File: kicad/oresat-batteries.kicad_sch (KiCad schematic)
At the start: 13 parts, among them J1 J-SAMTEC-TFM-120-X1-XXX-D-RA, SW1 Omron D2F-L3-D (LEFT), SW2 Omron D2F-L3-D (RIGHT), SW3 OMRON D2F-L3-D (LEFT), SW4 OMRON D2F-L3-D (RIGHT)

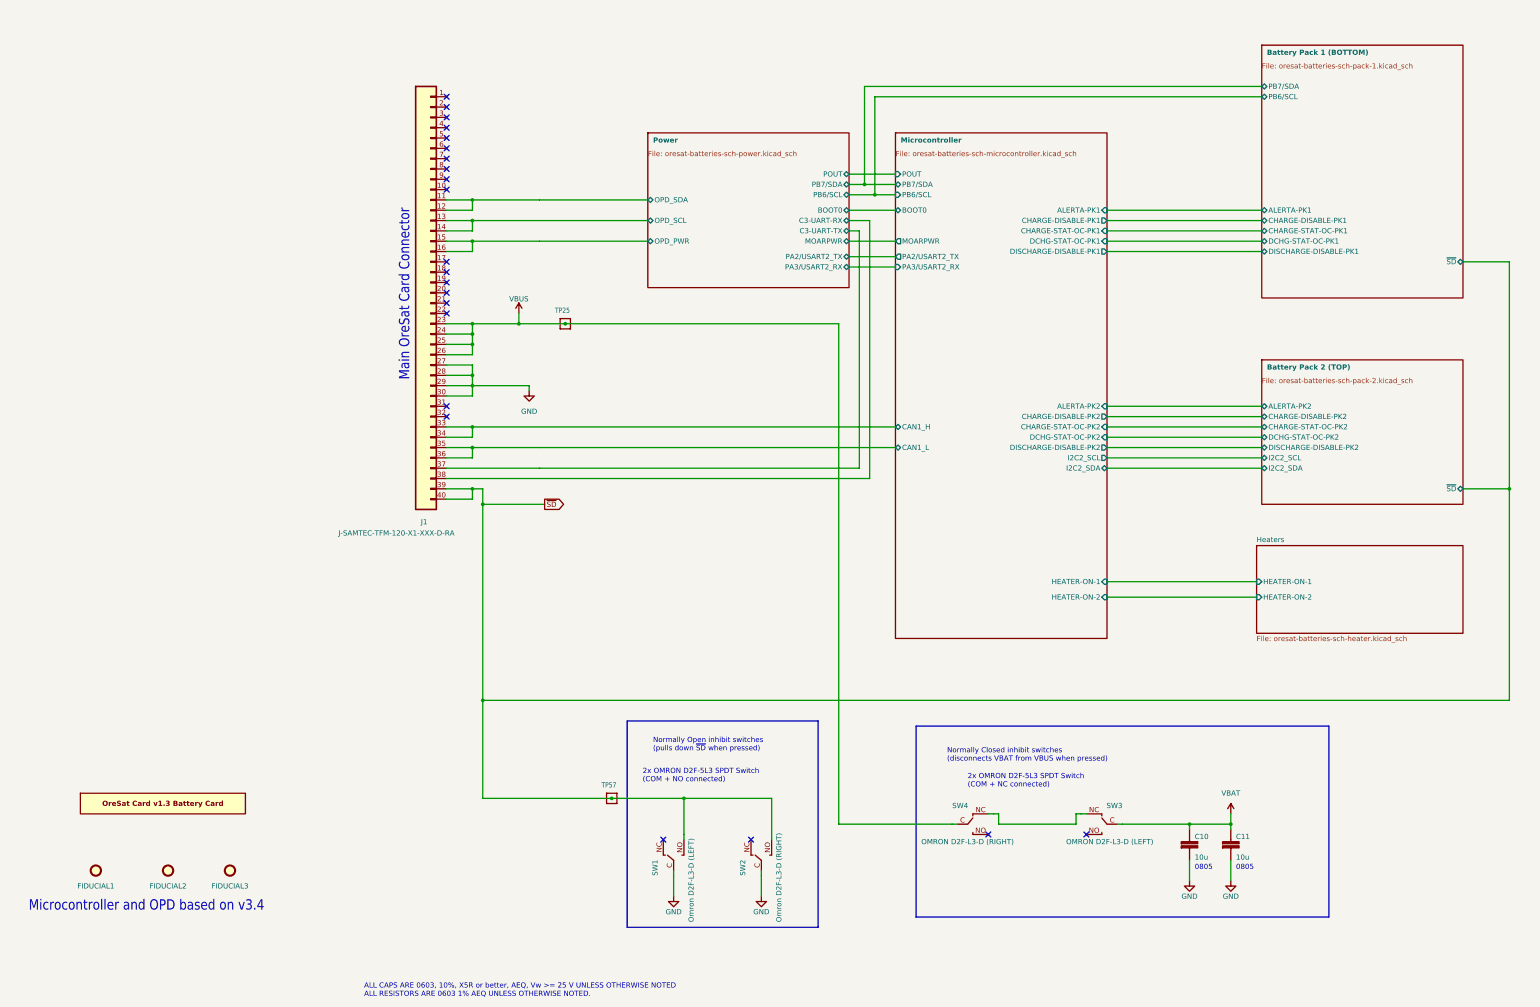
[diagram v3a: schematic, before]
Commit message: Minor polishing, removing outdated OPD signals and OPD power jumper.
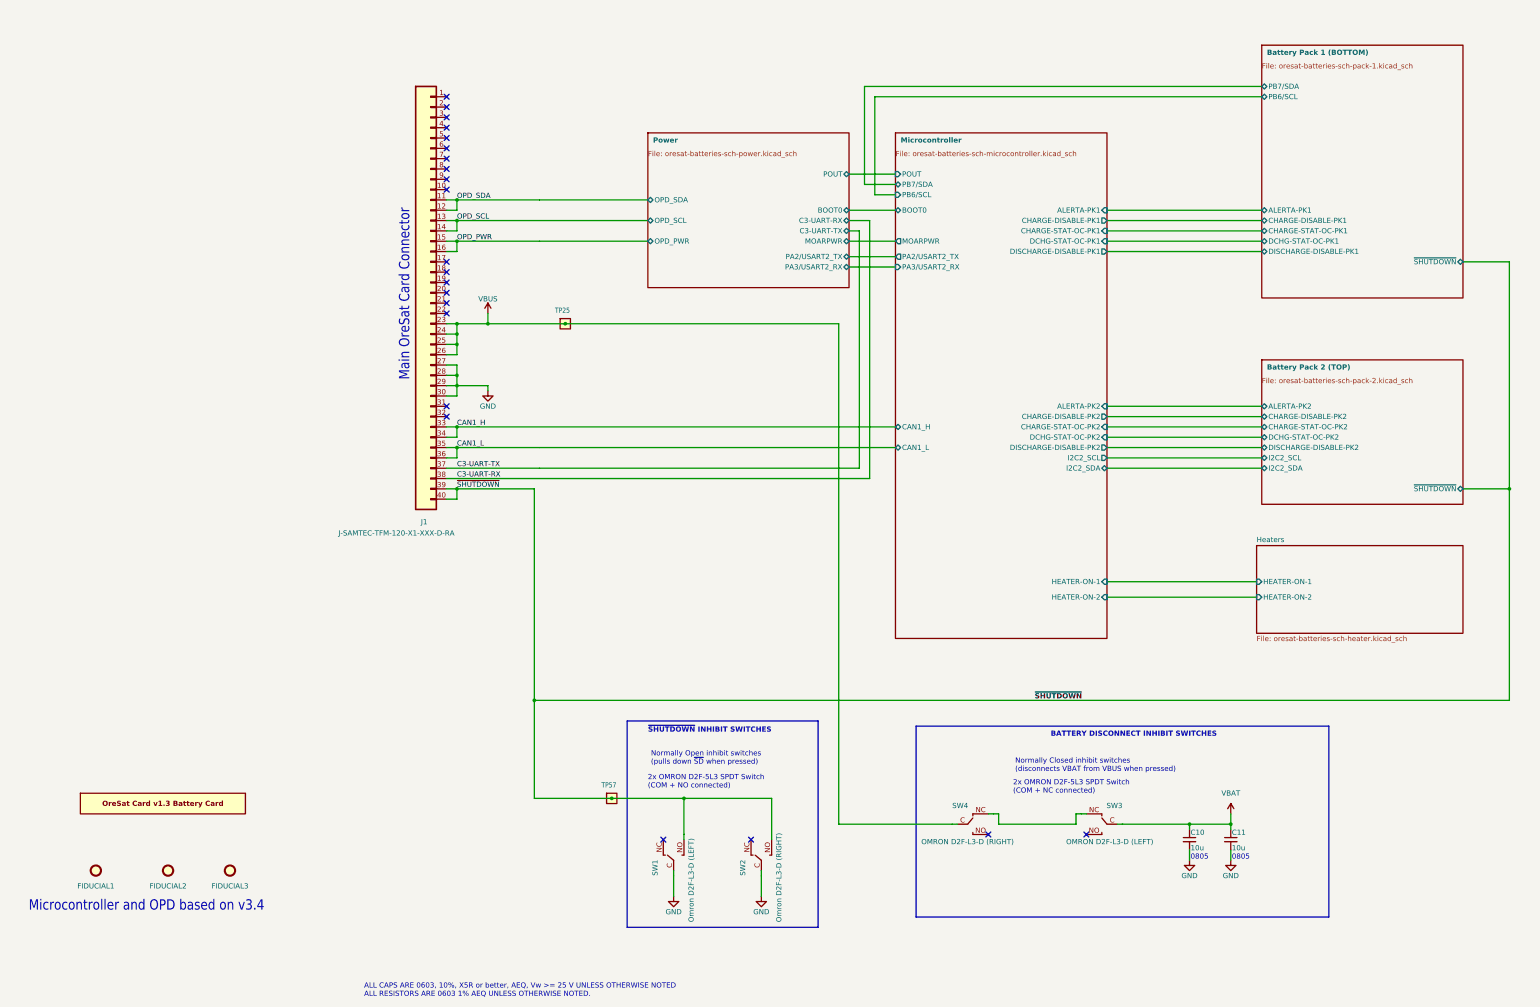
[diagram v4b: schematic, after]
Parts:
- C10, C11: symbol oresat-batteries-eagle-import:C-EU0805-B-NOSILK -> Device:C_Small
- TP25, TP57: footprint oresat-batteries:1X01 -> oresat-misc:TestPoint-0.75mm-th; symbol oresat-batteries-eagle-import:TEST-POINT-LARGE-SQUARE -> oresat-misc:Test-Point-0.75mm-th; now left out of the parts list
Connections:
- net Microcontroller/CAN1_H renamed CAN1_H
- net Microcontroller/CAN1_L renamed CAN1_L
- net Power/C3-UART-RX renamed C3-UART-RX
- net Power/C3-UART-TX renamed C3-UART-TX
- net Power/OPD_PWR renamed OPD_PWR
- net Power/OPD_SCL renamed OPD_SCL
- net Power/OPD_SDA renamed OPD_SDA
- net ~{SD} renamed ~{SHUTDOWN}
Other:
- sheet Battery Pack 1 (BOTTOM) ports: added ~{SHUTDOWN}; removed ~{SD}
- sheet Battery Pack 2 (TOP) ports: added ~{SHUTDOWN}; removed ~{SD}
- sheet Power ports: added none; removed PB6/SCL, PB7/SDA
- note added: "BATTERY DISCONNECT INHIBIT SWITCHES"
- note added: "~{SHUTDOWN} INHIBIT SWITCHES"

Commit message: Added +battery disconect mosfet and switch
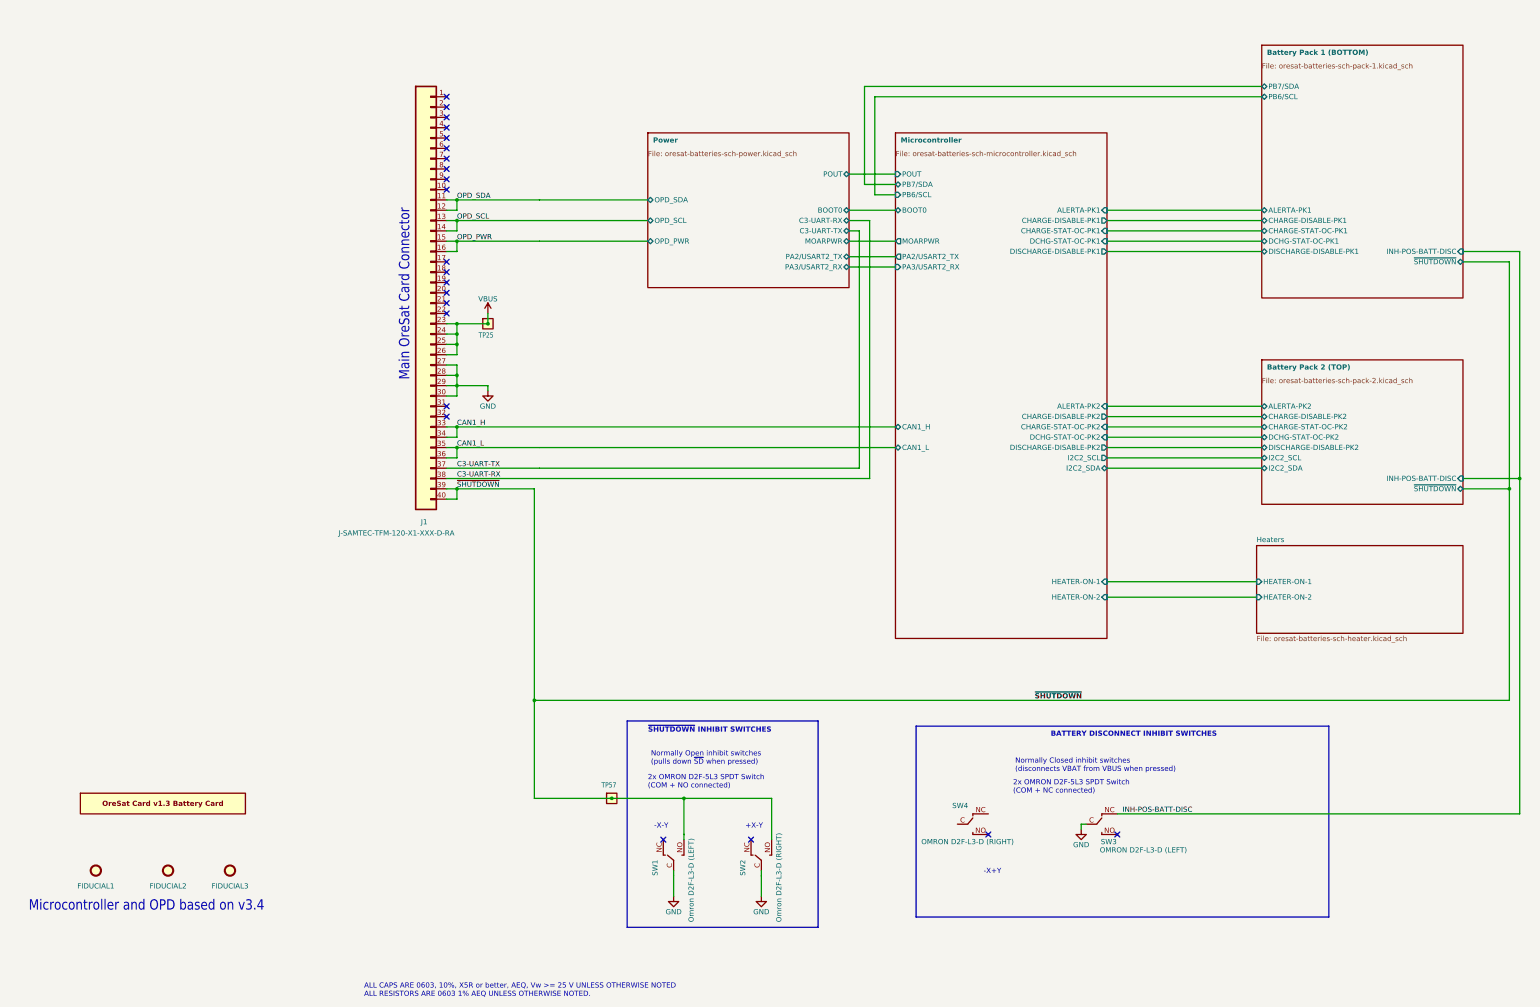
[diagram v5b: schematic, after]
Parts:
- removed C10, C11: 10u, oresat-batteries:.0805-B-NOSILK, symbol Device:C_Small
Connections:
- net VBAT is gone; now on net GND: SW3.C (COM)
- net VBUS: no longer SW4.C (COM)
- net at SW4.NC: no longer SW3.NC
- new net INH-POS-BATT-DISC: SW3.NC
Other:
- sheet Battery Pack 1 (BOTTOM) ports: added INH-POS-BATT-DISC; removed none
- sheet Battery Pack 2 (TOP) ports: added INH-POS-BATT-DISC; removed none
- note added: "+X-Y"
- note added: "-X+Y"
- note added: "-X-Y"
- note removed: "0805"
- moved on the sheet: TP25
